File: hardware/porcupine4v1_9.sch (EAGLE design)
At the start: 33 parts, among them X1 PROGCON

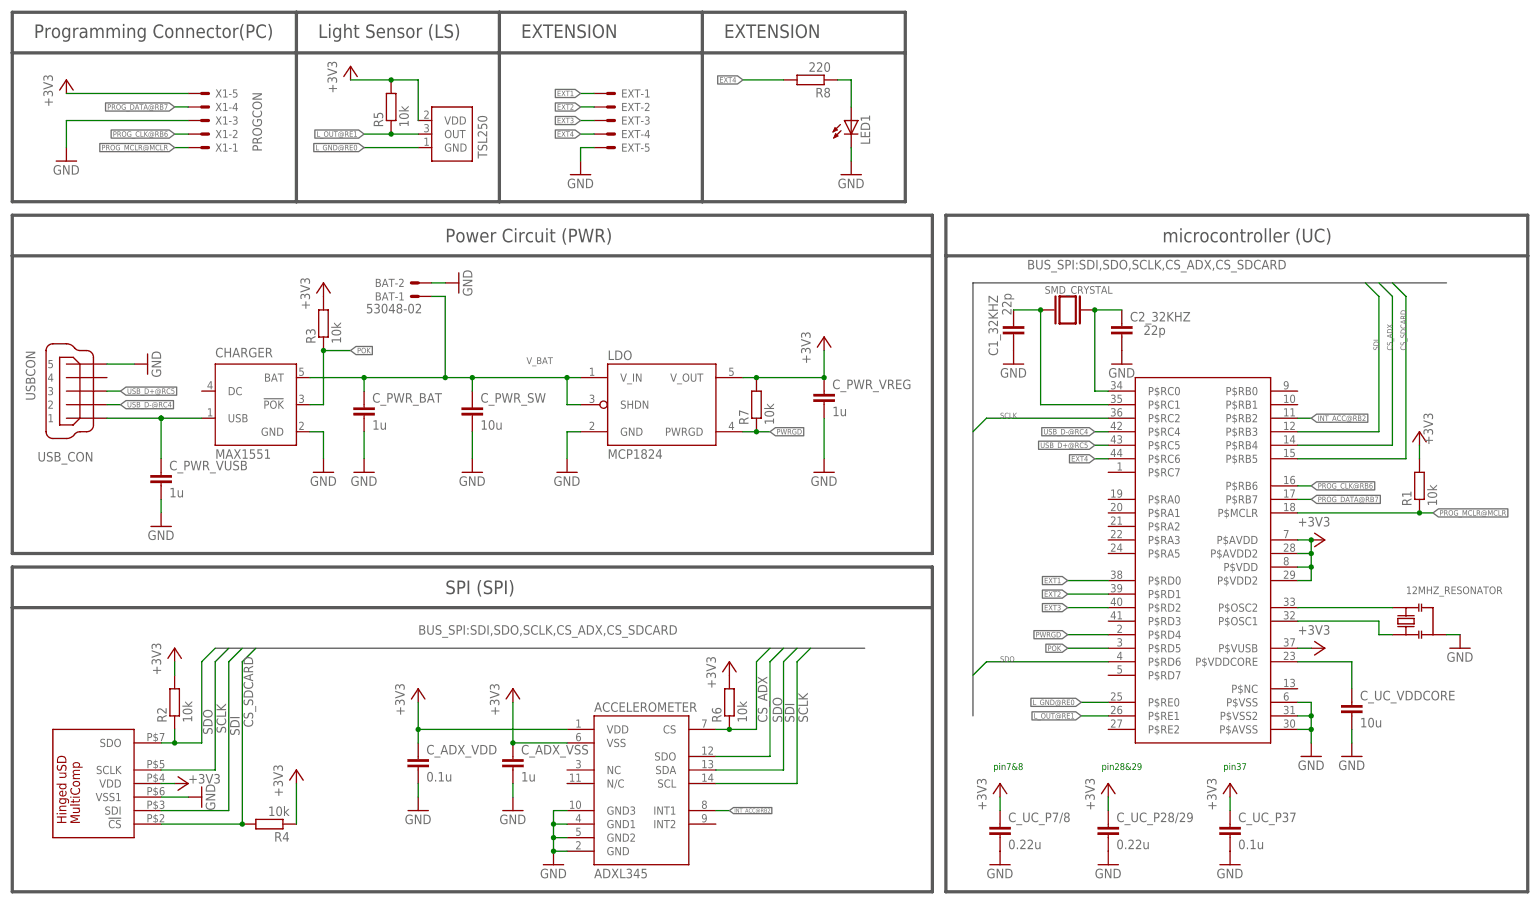
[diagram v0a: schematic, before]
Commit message: updated porcupine4v1_9 for better placement of components; removed PWRGD
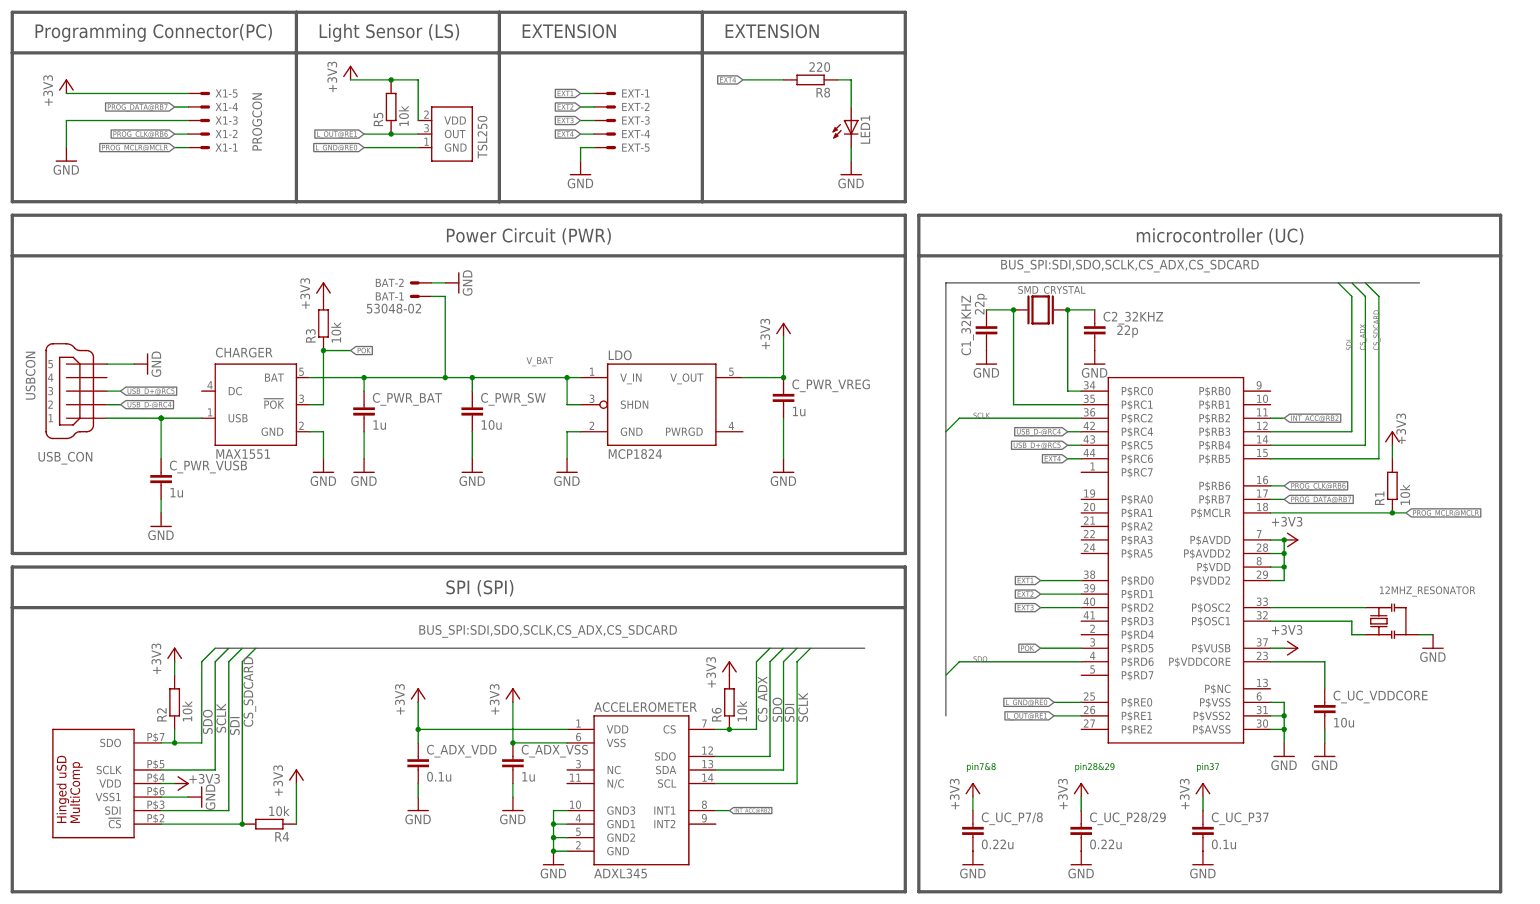
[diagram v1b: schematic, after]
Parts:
- removed R7: 10k, rcl:R-EU_R0603
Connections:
- removed net PWRGD: LDO.PWRGD, PIC_CONTROLLER.P$RD4, R7.1
- net +3V3: no longer R7.2
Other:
- moved on the sheet: 12MHZ_RESONATOR, C1_32KHZ, C2_32KHZ, C_PWR_VREG, C_UC_P28/29, C_UC_P37, C_UC_P7/8, C_UC_VDDCORE, R1

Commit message: updated basic 4.1.9
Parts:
- removed EXT: PROGCON, HedgehogLib:PROGCON
- removed LED1: (no value), led:LEDSML0805
- removed R8: 220, rcl:R-EU_R0603
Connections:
- removed net EXT1: EXT-1.S, PIC_CONTROLLER.P$RD0
- removed net EXT2: EXT-2.S, PIC_CONTROLLER.P$RD1
- removed net EXT3: EXT-3.S, PIC_CONTROLLER.P$RD2
- removed net EXT4: EXT-4.S, PIC_CONTROLLER.P$RC6, R8.2
- removed net N$4: LED1.A, R8.1
- net GND: no longer EXT-5.S, LED1.C
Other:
- note removed: "EXTENSION"
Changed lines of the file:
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@@
 <part name="LDO" library="HedgehogLib" deviceset="MCP1824" device=""/>
 <part name="BAT" library="con-molex" deviceset="53?-02" device="048"/>
-<part name="EXT" library="HedgehogLib" deviceset="PROGCON" device=""/>
-<part name="R8" library="rcl" deviceset="R-EU_" device="R0603" value="220"/>
-<part name="GND2" library="supply1" deviceset="GND" device=""/>
-<part name="LED1" library="led" deviceset="LED" device="SML0805"/>
-<part name="GND10" library="supply1" deviceset="GND" device=""/>
 <part name="12MHZ_RESONATOR" library="HedgehogLib" deviceset="RESONATOR" device="PRQC-C">
 <attribute name="DIGIKEY" value="http://www.digikey.de/product-detail/de/PRQC12.00CR5010X000/478-6318-1-ND/2506334"/>
@@
 <text x="59.944" y="162.814" size="2.54" layer="97">Light Sensor (LS)</text>
 <text x="181.61" y="25.4" size="1.27" layer="91">pin7&amp;8</text>
-<wire x1="93.98" y1="167.64" x2="132.08" y2="167.64" width="0.6096" layer="97"/>
-<wire x1="132.08" y1="160.02" x2="132.08" y2="167.64" width="0.6096" layer="97"/>
-<wire x1="93.98" y1="160.02" x2="132.08" y2="160.02" width="0.6096" layer="97"/>
-<wire x1="132.08" y1="132.08" x2="132.08" y2="160.02" width="0.6096" layer="97"/>
-<wire x1="93.98" y1="132.08" x2="132.08" y2="132.08" width="0.6096" layer="97"/>
-<text x="98.044" y="162.814" size="2.54" layer="97">EXTENSION</text>
-<wire x1="132.08" y1="167.64" x2="170.18" y2="167.64" width="0.6096" layer="97"/>
-<wire x1="170.18" y1="160.02" x2="170.18" y2="167.64" width="0.6096" layer="97"/>
-<wire x1="132.08" y1="160.02" x2="170.18" y2="160.02" width="0.6096" layer="97"/>
-<wire x1="170.18" y1="132.08" x2="170.18" y2="160.02" width="0.6096" layer="97"/>
-<wire x1="132.08" y1="132.08" x2="170.18" y2="132.08" width="0.6096" layer="97"/>
-<text x="136.144" y="162.814" size="2.54" layer="97">EXTENSION</text>
 </plain>
 <instances>
@@
 <instance part="BAT" gate="-1" x="78.74" y="114.3" rot="R180"/>
 <instance part="BAT" gate="-2" x="78.74" y="116.84" rot="R180"/>
-<instance part="EXT" gate="-1" x="114.3" y="152.4" smashed="yes">
-<attribute name="NAME" x="116.84" y="151.638" size="1.524" layer="95"/>
-</instance>
-<instance part="EXT" gate="-2" x="114.3" y="149.86"/>
-<instance part="EXT" gate="-3" x="114.3" y="147.32"/>
-<instance part="EXT" gate="-4" x="114.3" y="144.78"/>
-<instance part="EXT" gate="-5" x="114.3" y="142.24"/>
-<instance part="R8" gate="G$1" x="152.4" y="154.94" rot="R180"/>
-<instance part="GND2" gate="1" x="160.02" y="137.16"/>
-<instance part="LED1" gate="G$1" x="160.02" y="147.32"/>
-<instance part="GND10" gate="1" x="109.22" y="137.16"/>
 <instance part="12MHZ_RESONATOR" gate="RESONATOR" x="259.08" y="53.34" smashed="yes" rot="R180">
 <attribute name="DIGIKEY" x="259.08" y="53.34" size="1.778" layer="96" rot="R180" display="off"/>
@@
 <wire x1="266.7" y1="50.8" x2="269.24" y2="50.8" width="0.1524" layer="91"/>
 <pinref part="12MHZ_RESONATOR" gate="RESONATOR" pin="GND"/>
-</segment>
-<segment>
-<pinref part="LED1" gate="G$1" pin="C"/>
-<pinref part="GND2" gate="1" pin="GND"/>
-<wire x1="160.02" y1="139.7" x2="160.02" y2="142.24" width="0.1524" layer="91"/>
-</segment>
-<segment>
-<pinref part="EXT" gate="-5" pin="S"/>
-<wire x1="111.76" y1="142.24" x2="109.22" y2="142.24" width="0.1524" layer="91"/>
-<pinref part="GND10" gate="1" pin="GND"/>
-<wire x1="109.22" y1="139.7" x2="109.22" y2="142.24" width="0.1524" layer="91"/>
 </segment>
 </net>
@@
 </segment>
 </net>
-<net name="EXT1" class="0">
-<segment>
-<pinref part="EXT" gate="-1" pin="S"/>
-<wire x1="111.76" y1="152.4" x2="109.22" y2="152.4" width="0.1524" layer="91"/>
-<label x="109.22" y="152.4" size="1.016" layer="95" rot="R180" xref="yes"/>
-</segment>
-<segment>
-<pinref part="PIC_CONTROLLER" gate="G$1" pin="P$RD0"/>
-<wire x1="203.2" y1="60.96" x2="195.58" y2="60.96" width="0.1524" layer="91"/>
-<label x="195.58" y="60.96" size="1.016" layer="95" rot="R180" xref="yes"/>
-</segment>
-</net>
-<net name="EXT2" class="0">
-<segment>
-<pinref part="EXT" gate="-2" pin="S"/>
-<wire x1="111.76" y1="149.86" x2="109.22" y2="149.86" width="0.1524" layer="91"/>
-<label x="109.22" y="149.86" size="1.016" layer="95" rot="R180" xref="yes"/>
-</segment>
-<segment>
-<pinref part="PIC_CONTROLLER" gate="G$1" pin="P$RD1"/>
-<wire x1="203.2" y1="58.42" x2="195.58" y2="58.42" width="0.1524" layer="91"/>
-<label x="195.58" y="58.42" size="1.016" layer="95" rot="R180" xref="yes"/>
-</segment>
-</net>
-<net name="EXT3" class="0">
-<segment>
-<pinref part="EXT" gate="-3" pin="S"/>
-<wire x1="111.76" y1="147.32" x2="109.22" y2="147.32" width="0.1524" layer="91"/>
-<label x="109.22" y="147.32" size="1.016" layer="95" rot="R180" xref="yes"/>
-</segment>
-<segment>
-<pinref part="PIC_CONTROLLER" gate="G$1" pin="P$RD2"/>
-<wire x1="203.2" y1="55.88" x2="195.58" y2="55.88" width="0.1524" layer="91"/>
-<label x="195.58" y="55.88" size="1.016" layer="95" rot="R180" xref="yes"/>
-</segment>
-</net>
-<net name="N$4" class="0">
-<segment>
-<pinref part="LED1" gate="G$1" pin="A"/>
-<pinref part="R8" gate="G$1" pin="1"/>
-<wire x1="157.48" y1="154.94" x2="160.02" y2="154.94" width="0.1524" layer="91"/>
-<wire x1="160.02" y1="154.94" x2="160.02" y2="149.86" width="0.1524" layer="91"/>
-</segment>
-</net>
-<net name="EXT4" class="0">
-<segment>
-<pinref part="PIC_CONTROLLER" gate="G$1" pin="P$RC6"/>
-<wire x1="203.2" y1="83.82" x2="200.66" y2="83.82" width="0.1524" layer="91"/>
-<label x="200.66" y="83.82" size="1.016" layer="95" rot="R180" xref="yes"/>
-</segment>
-<segment>
-<wire x1="111.76" y1="144.78" x2="109.22" y2="144.78" width="0.1524" layer="91"/>
-<label x="109.22" y="144.78" size="1.016" layer="95" rot="R180" xref="yes"/>
-<pinref part="EXT" gate="-4" pin="S"/>
-</segment>
-<segment>
-<wire x1="147.32" y1="154.94" x2="139.7" y2="154.94" width="0.1524" layer="91"/>
-<label x="139.7" y="154.94" size="1.016" layer="95" rot="R180" xref="yes"/>
-<pinref part="R8" gate="G$1" pin="2"/>
-</segment>
-</net>

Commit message: eagle design update basic 4.1.9
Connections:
- net V_USB: now also CHARGER.DC
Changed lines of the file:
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@@
 <segment>
 <wire x1="30.48" y1="83.82" x2="30.48" y2="91.44" width="0.1524" layer="91"/>
-<wire x1="38.1" y1="91.44" x2="30.48" y2="91.44" width="0.1524" layer="91"/>
+<wire x1="38.1" y1="91.44" x2="35.56" y2="91.44" width="0.1524" layer="91"/>
+<wire x1="35.56" y1="91.44" x2="30.48" y2="91.44" width="0.1524" layer="91"/>
 <wire x1="20.32" y1="91.44" x2="30.48" y2="91.44" width="0.1524" layer="91"/>
 <junction x="30.48" y="91.44"/>
@@
 <pinref part="CHARGER" gate="G$1" pin="USB"/>
 <pinref part="USB_CON" gate="G$1" pin="1"/>
+<wire x1="35.56" y1="91.44" x2="35.56" y2="96.52" width="0.1524" layer="91"/>
+<pinref part="CHARGER" gate="G$1" pin="DC"/>
+<wire x1="35.56" y1="96.52" x2="38.1" y2="96.52" width="0.1524" layer="91"/>
 </segment>
 </net>
